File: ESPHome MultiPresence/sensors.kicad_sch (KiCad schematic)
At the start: 7 parts, among them U2 SEN0395, U3 EKMC1603113, U4 TSL2591, U5 BME280

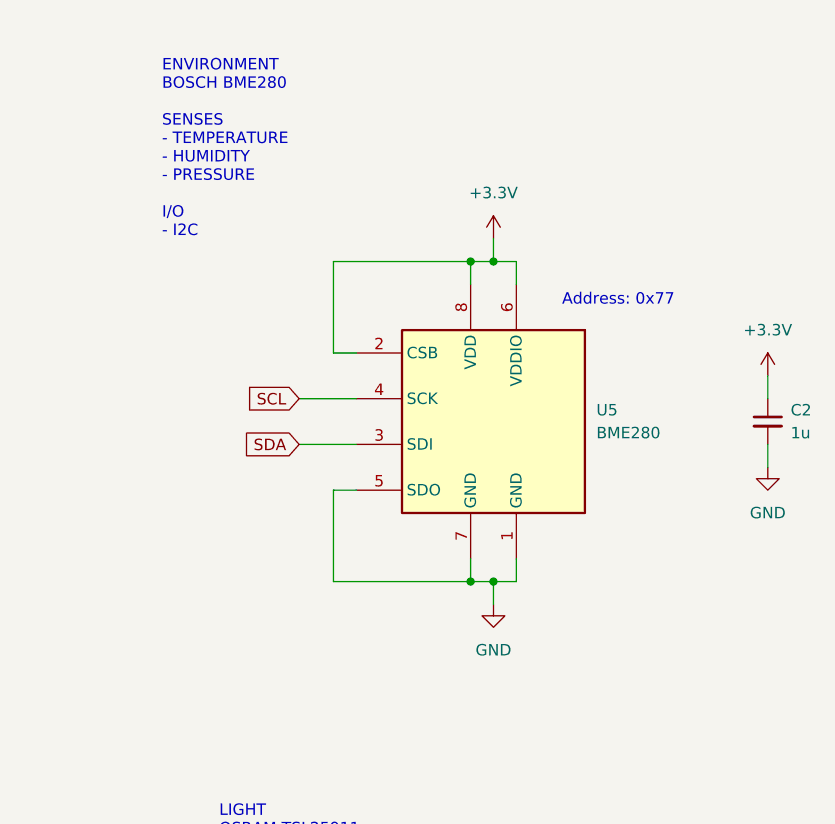
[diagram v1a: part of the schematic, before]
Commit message: replaced J3 with pinheadder, fixed USB-C footprint pin assignment
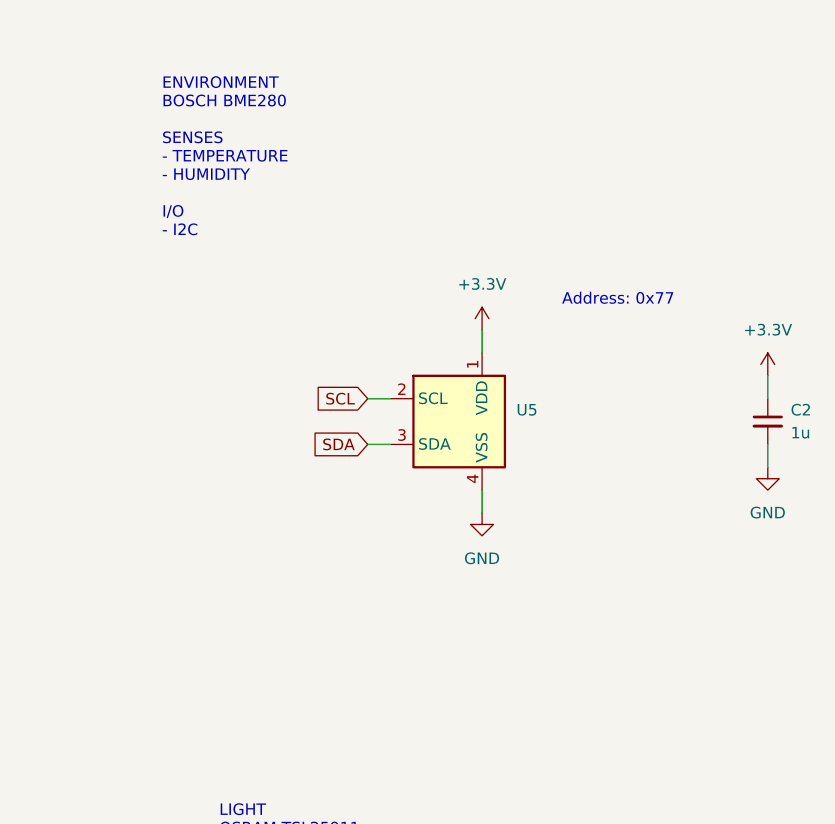
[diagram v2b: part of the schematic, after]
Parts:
- removed U5: BME280, Package_LGA:Bosch_LGA-8_2.5x2.5mm_P0.65mm_ClockwisePinNumbering, symbol Sensor:BME280
- added U5: (no value), symbol Sensor_Humidity:SHTC3
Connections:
- net +3.3V: now also U5.1 (VDD)
- net GND: now also U5.4 (VSS)
- net SCL: now also U5.2 (SCL)
- net SDA: now also U5.3 (SDA)
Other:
- note added: "ENVIRONMENT BOSCH BME280 SENSES - TEMPERATURE - HUMIDITY I/O - I2C"
- note removed: "ENVIRONMENT BOSCH BME280 SENSES - TEMPERATURE - HUMIDITY - PRESSURE I/O - I2C"
